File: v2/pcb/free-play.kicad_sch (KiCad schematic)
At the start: 15 parts

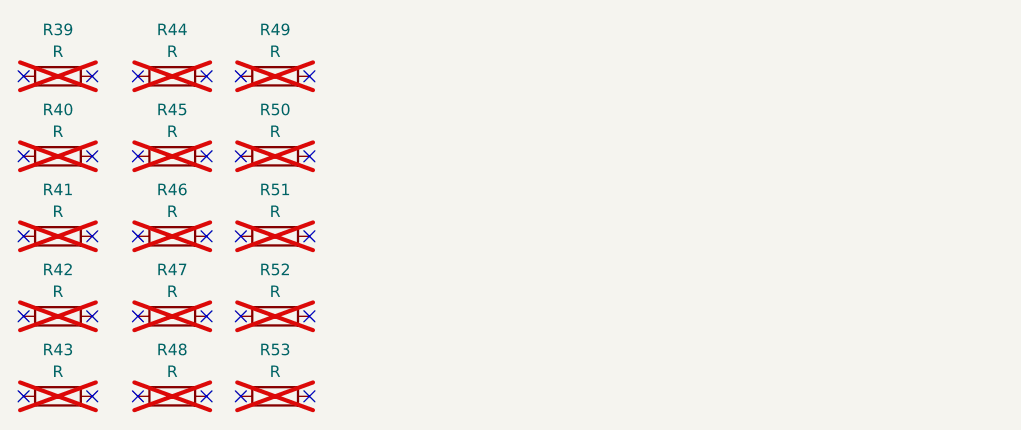
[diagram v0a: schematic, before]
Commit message: Added more inner layer test features to free play area
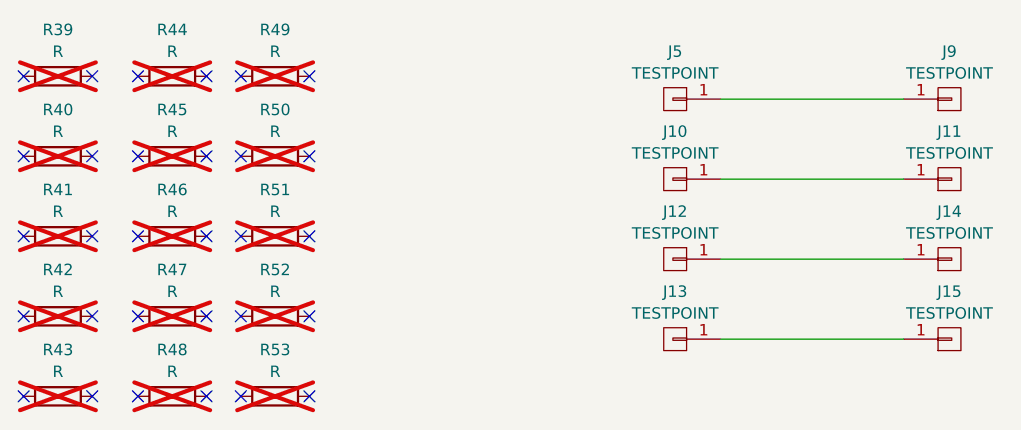
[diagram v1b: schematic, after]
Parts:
- added J10, J11, J12, J13, J14, J15, J5, J9: TESTPOINT, azonenberg_pcb:TESTPOINT_SMT_0.5MM, symbol conn:CONN_01X01
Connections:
- new net: J5.1 (P1), J9.1 (P1)
- new net: J12.1 (P1), J14.1 (P1)
- new net: J10.1 (P1), J11.1 (P1)
- new net: J13.1 (P1), J15.1 (P1)
